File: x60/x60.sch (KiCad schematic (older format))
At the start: 1 part

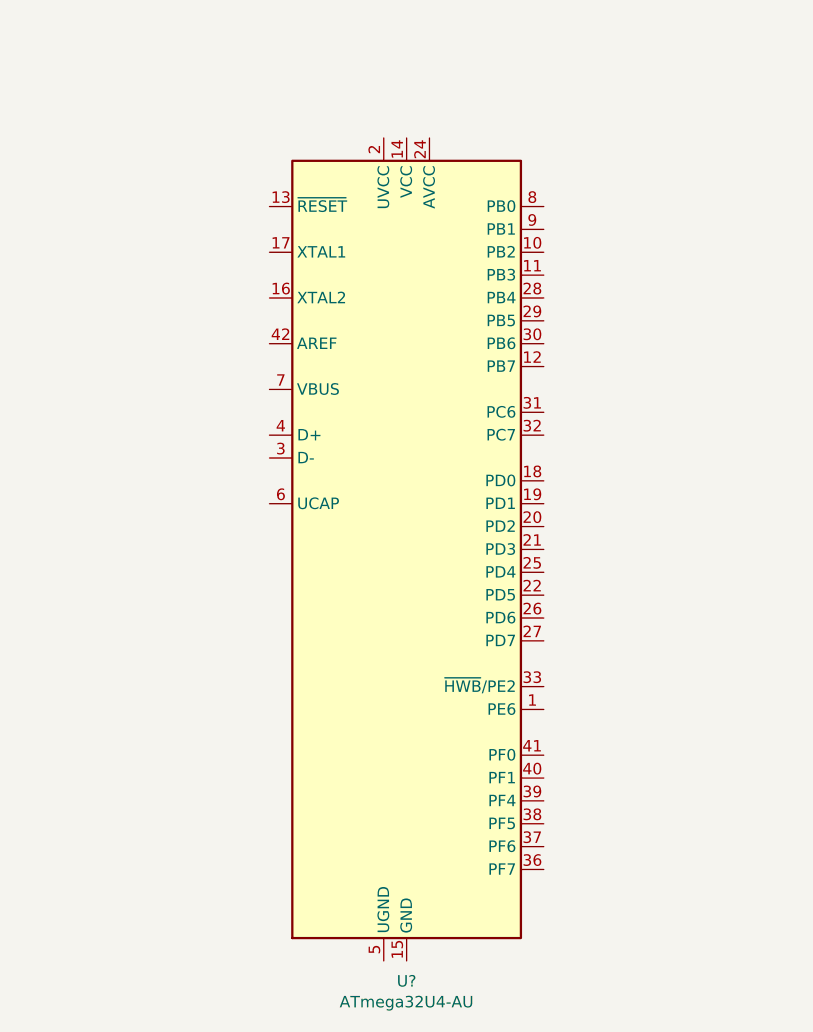
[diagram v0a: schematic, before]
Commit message: wired mcu
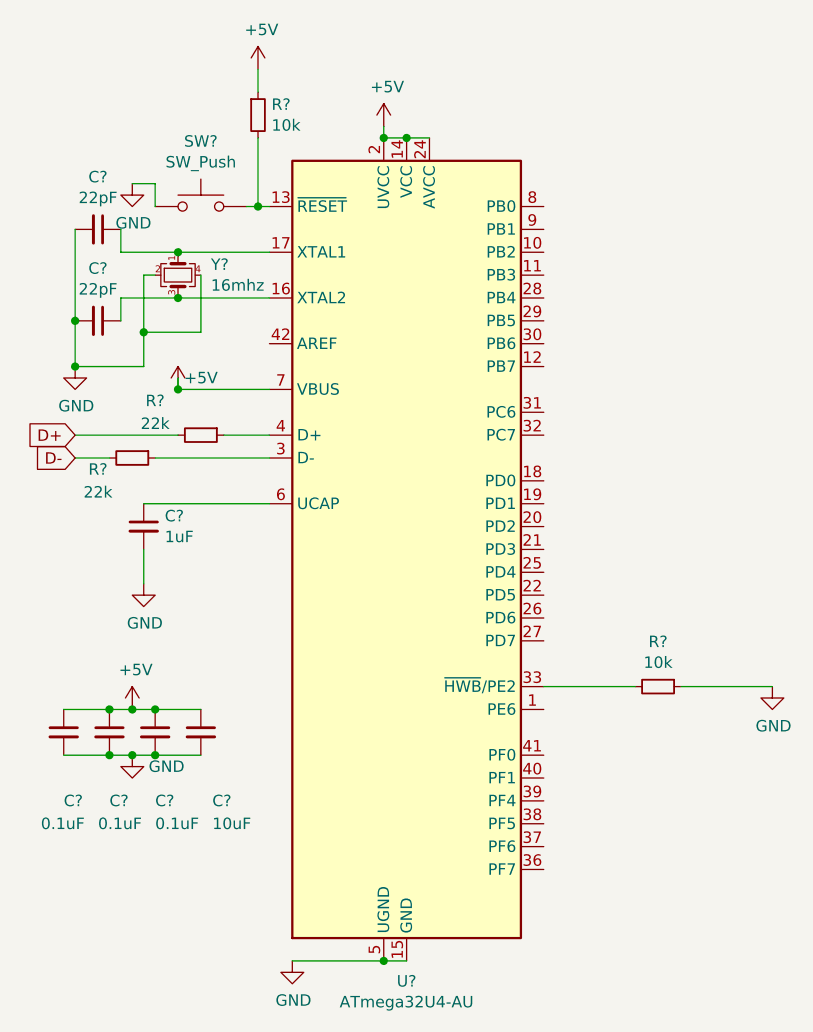
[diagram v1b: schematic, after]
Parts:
- added C?: 1uF, symbol Device:C_Small
- added C? (x3): 0.1uF, symbol Device:C_Small
- added C?: 10uF, symbol Device:C_Small
- added C? (x2): 22pF, symbol Device:C_Small
- added R? (x2): 10k, symbol Device:R_Small
- added R? (x2): 22k, symbol Device:R_Small
- added SW?: SW_Push, symbol Switch:SW_Push
- added Y?: 16mhz, symbol Device:Crystal_GND24_Small
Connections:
- net at U?.13 (~RESET): now also R?.2, SW?.2
- net +5V: now reaches U?.14 (VCC), U?.34 (VCC)
- net +5V: now also U?.2 (UVCC), U?.24 (AVCC), U?.44 (AVCC), U?.7 (VBUS), C?.1, C?.1, C?.1, C?.1, R?.1
- net GND: now reaches U?.15 (GND), U?.23 (GND), U?.35 (GND), U?.43 (GND)
- net GND: now also U?.5 (UGND), C?.2, C?.2, C?.2, C?.2, C?.2, C?.2, C?.2, R?.1, SW?.1, Y?.2, Y?.4
- net at U?.16 (XTAL2): now also C?.1, Y?.3
- net at U?.17 (XTAL1): now also C?.1, Y?.1
- net at U?.3 (D-): now also R?.1
- net at U?.33 (~HWB~/PE2): now also R?.2
- net at U?.4 (D+): now also R?.1
- net at U?.6 (UCAP): now also C?.1
- new net D+: R?.2
- new net D-: R?.2

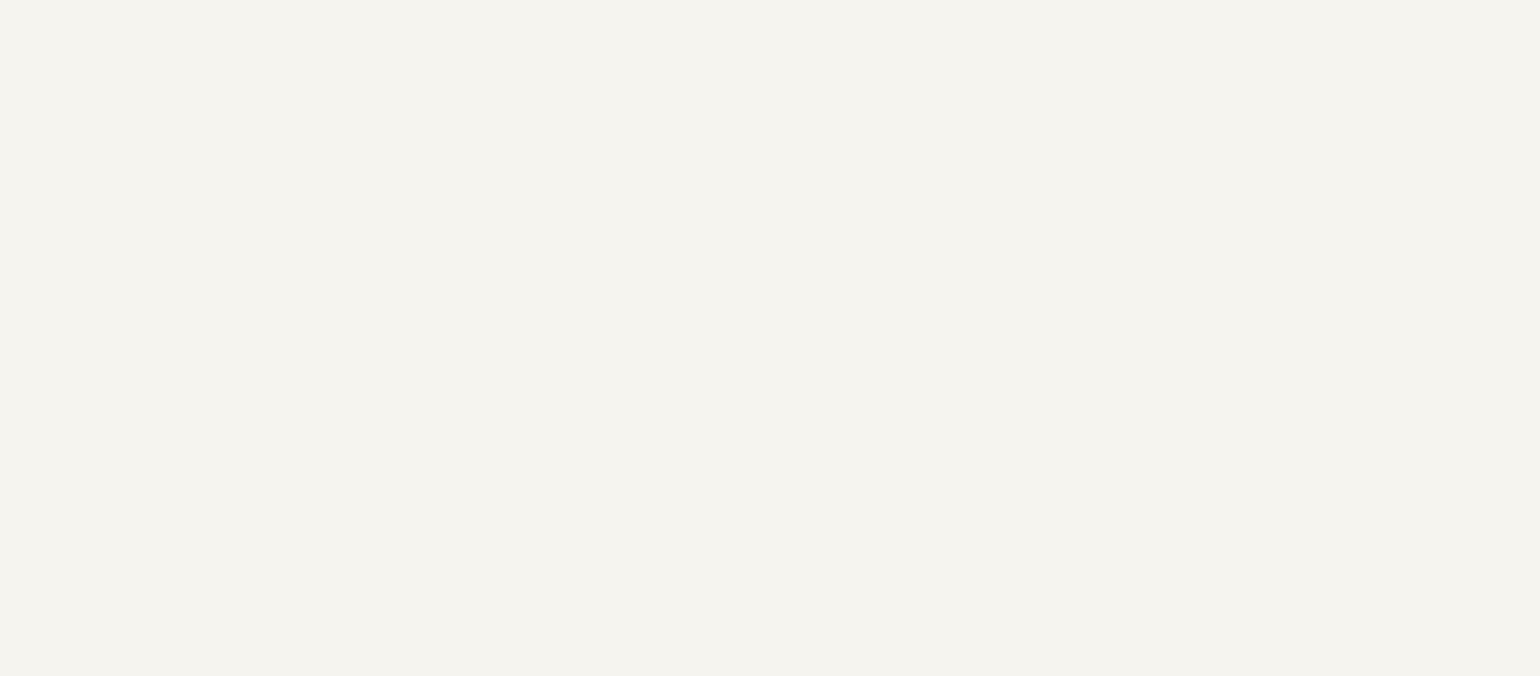
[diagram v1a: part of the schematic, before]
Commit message: added switches
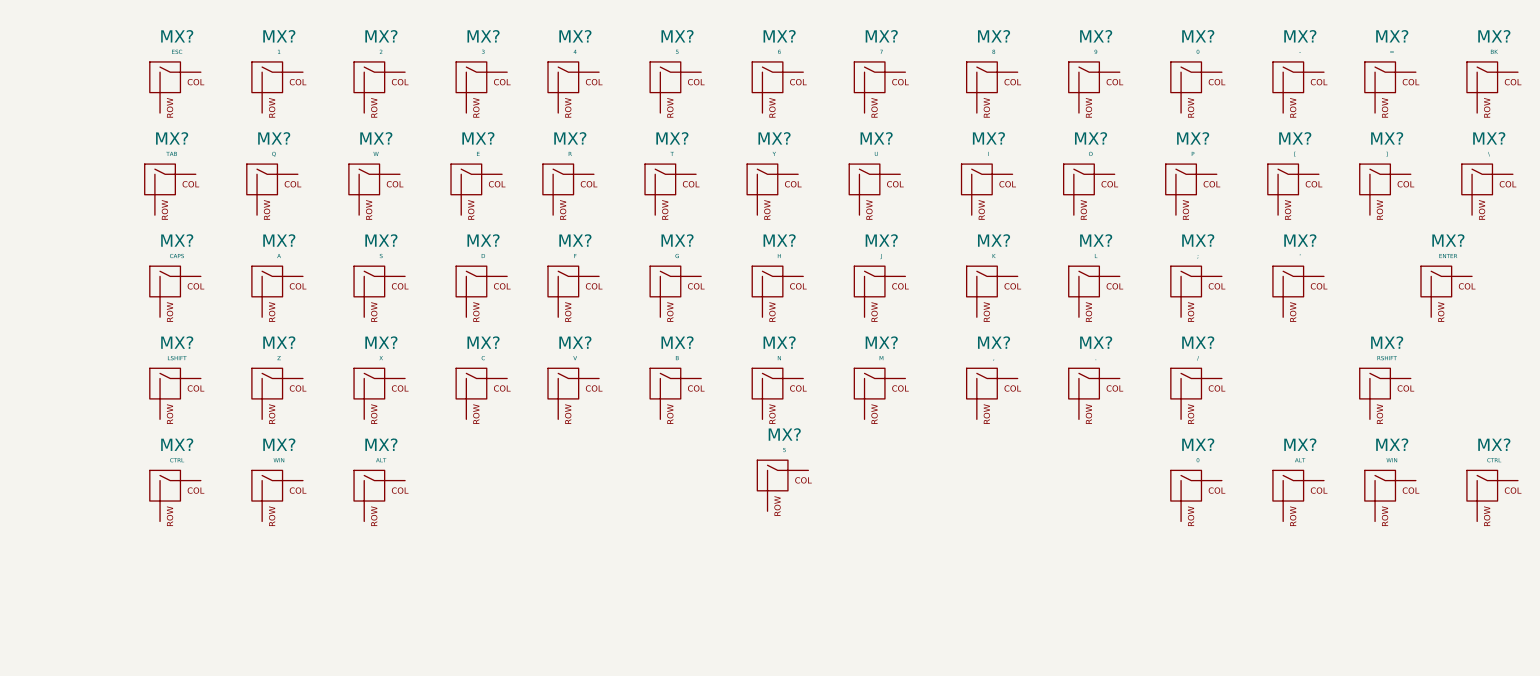
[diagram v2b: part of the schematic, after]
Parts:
- added MX?: ESC, symbol MX_Alps_Hybrid:MX-NoLED
- added MX?: 1, symbol MX_Alps_Hybrid:MX-NoLED
- added MX?: 2, symbol MX_Alps_Hybrid:MX-NoLED
- added MX?: 3, symbol MX_Alps_Hybrid:MX-NoLED
- added MX?: 4, symbol MX_Alps_Hybrid:MX-NoLED
- added MX? (x2): 5, symbol MX_Alps_Hybrid:MX-NoLED
- added MX?: 6, symbol MX_Alps_Hybrid:MX-NoLED
- added MX?: 7, symbol MX_Alps_Hybrid:MX-NoLED
- added MX?: 8, symbol MX_Alps_Hybrid:MX-NoLED
- added MX?: 9, symbol MX_Alps_Hybrid:MX-NoLED
- added MX? (x2): 0, symbol MX_Alps_Hybrid:MX-NoLED
- added MX?: -, symbol MX_Alps_Hybrid:MX-NoLED
- added MX?: =, symbol MX_Alps_Hybrid:MX-NoLED
- added MX?: BK, symbol MX_Alps_Hybrid:MX-NoLED
- added MX?: TAB, symbol MX_Alps_Hybrid:MX-NoLED
- added MX?: Q, symbol MX_Alps_Hybrid:MX-NoLED
- added MX?: W, symbol MX_Alps_Hybrid:MX-NoLED
- added MX?: E, symbol MX_Alps_Hybrid:MX-NoLED
- added MX?: R, symbol MX_Alps_Hybrid:MX-NoLED
- added MX?: T, symbol MX_Alps_Hybrid:MX-NoLED
- added MX?: Y, symbol MX_Alps_Hybrid:MX-NoLED
- added MX?: U, symbol MX_Alps_Hybrid:MX-NoLED
- added MX?: I, symbol MX_Alps_Hybrid:MX-NoLED
- added MX?: O, symbol MX_Alps_Hybrid:MX-NoLED
- added MX?: P, symbol MX_Alps_Hybrid:MX-NoLED
- added MX?: [, symbol MX_Alps_Hybrid:MX-NoLED
- added MX?: ], symbol MX_Alps_Hybrid:MX-NoLED
- added MX?: \\, symbol MX_Alps_Hybrid:MX-NoLED
- added MX?: CAPS, symbol MX_Alps_Hybrid:MX-NoLED
- added MX?: A, symbol MX_Alps_Hybrid:MX-NoLED
- added MX?: S, symbol MX_Alps_Hybrid:MX-NoLED
- added MX?: D, symbol MX_Alps_Hybrid:MX-NoLED
- added MX?: F, symbol MX_Alps_Hybrid:MX-NoLED
- added MX?: G, symbol MX_Alps_Hybrid:MX-NoLED
- added MX?: H, symbol MX_Alps_Hybrid:MX-NoLED
- added MX?: J, symbol MX_Alps_Hybrid:MX-NoLED
- added MX?: K, symbol MX_Alps_Hybrid:MX-NoLED
- added MX?: L, symbol MX_Alps_Hybrid:MX-NoLED
- added MX?: ;, symbol MX_Alps_Hybrid:MX-NoLED
- added MX?: ', symbol MX_Alps_Hybrid:MX-NoLED
- added MX?: ENTER, symbol MX_Alps_Hybrid:MX-NoLED
- added MX?: LSHIFT, symbol MX_Alps_Hybrid:MX-NoLED
- added MX?: Z, symbol MX_Alps_Hybrid:MX-NoLED
- added MX?: X, symbol MX_Alps_Hybrid:MX-NoLED
- added MX?: C, symbol MX_Alps_Hybrid:MX-NoLED
- added MX?: V, symbol MX_Alps_Hybrid:MX-NoLED
- added MX?: B, symbol MX_Alps_Hybrid:MX-NoLED
- added MX?: N, symbol MX_Alps_Hybrid:MX-NoLED
- added MX?: M, symbol MX_Alps_Hybrid:MX-NoLED
- added MX?: ,, symbol MX_Alps_Hybrid:MX-NoLED
- added MX?: ., symbol MX_Alps_Hybrid:MX-NoLED
- added MX?: /, symbol MX_Alps_Hybrid:MX-NoLED
- added MX?: RSHIFT, symbol MX_Alps_Hybrid:MX-NoLED
- added MX? (x2): CTRL, symbol MX_Alps_Hybrid:MX-NoLED
- added MX? (x2): WIN, symbol MX_Alps_Hybrid:MX-NoLED
- added MX? (x2): ALT, symbol MX_Alps_Hybrid:MX-NoLED

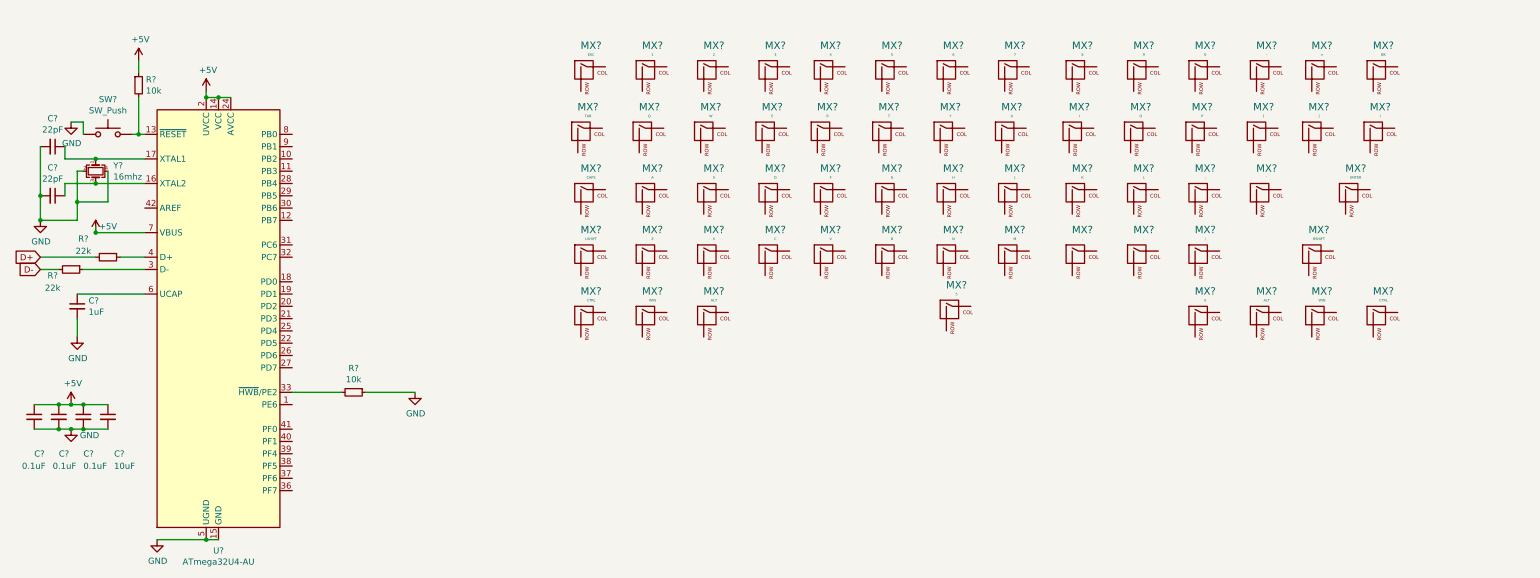
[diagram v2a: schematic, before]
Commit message: updated wiring
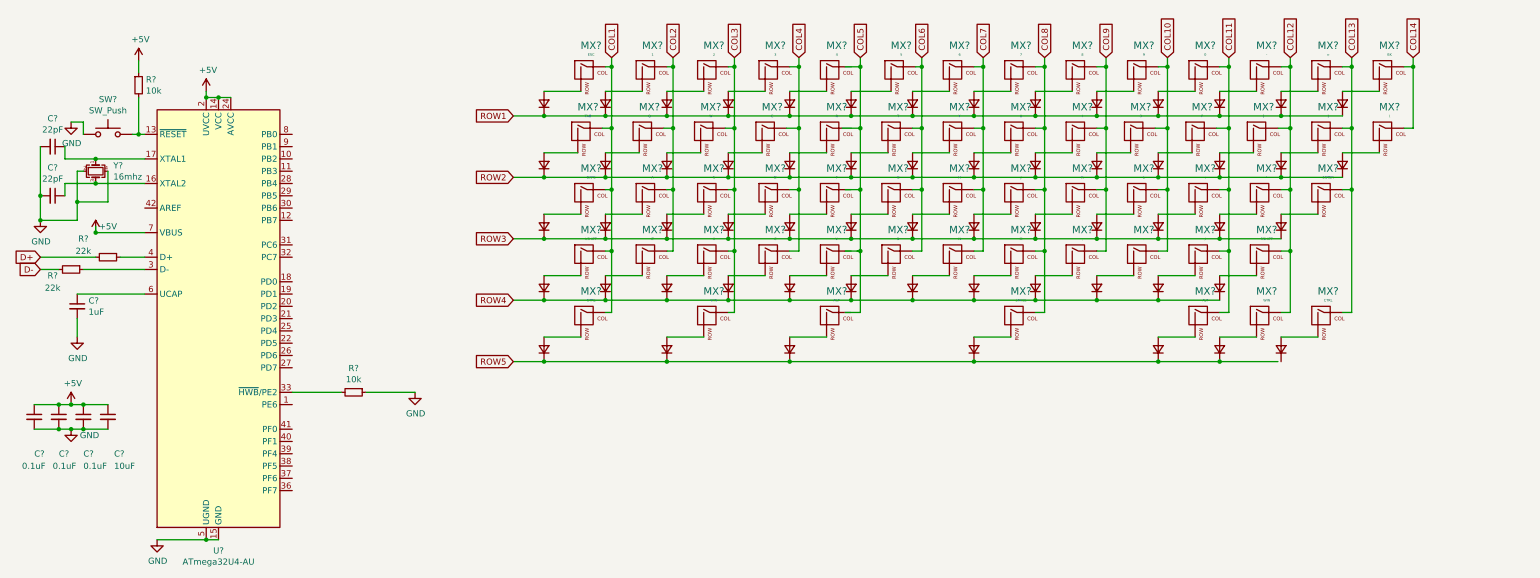
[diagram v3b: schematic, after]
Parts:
- removed MX?: 0, symbol MX_Alps_Hybrid:MX-NoLED
- added D? (x60): D_Small, symbol Device:D_Small
- MX?: value 5 -> SPACE
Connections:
- net labels added: COL1, COL10, COL11, COL12, COL13, COL14, COL2, COL3, COL4, COL5, COL6, COL7, COL8, COL9, ROW1, ROW2, ROW3, ROW4, ROW5
- wire segments 43 -> 284
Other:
- moved on the sheet: MX?

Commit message: added support for split rs/bs
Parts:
- added D61, D62: D_Small, symbol Device:D_Small
- added MX58: RSHIFT_1.75, symbol MX_Alps_Hybrid:MX-NoLED
- added MX62: FN, symbol MX_Alps_Hybrid:MX-NoLED
- added MX63: \\, symbol MX_Alps_Hybrid:MX-NoLED
- added MX64: `, symbol MX_Alps_Hybrid:MX-NoLED
- gave numbers to parts that had none: 134
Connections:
- wire segments 284 -> 302

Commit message: started designing pcb
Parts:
- C1, C2, C3, C4, C5, C6, C7: footprint (none) -> Capacitor_SMD:C_0805_2012Metric
- D1, D10, D11, D12, D13, D14, D15, D16, D17, D18, D19, D2, D20, D21, D22, D23, D24, D25, D26, D27, D28, D29, D3, D30, D31, D32, D33, D34, D35, D36, D37, D38, D39, D4, D40, D41, D42, D43, D44, D45, D46, D47, D48, D49, D5, D50, D51, D52, D53, D54, D55, D56, D57, D58, D59, D6, D60, D61, D62, D7, D8, D9: footprint (none) -> Diode_SMD:D_SOD-123
- MX1, MX10, MX11, MX12, MX13, MX14, MX15, MX16, MX17, MX18, MX19, MX2, MX20, MX21, MX22, MX23, MX24, MX25, MX26, MX27, MX28, MX29, MX3, MX30, MX31, MX32, MX33, MX34, MX35, MX36, MX37, MX38, MX39, MX4, MX40, MX41, MX42, MX43, MX44, MX45, MX46, MX47, MX48, MX49, MX5, MX50, MX51, MX52, MX53, MX54, MX55, MX56, MX57, MX58, MX59, MX6, MX60, MX61, MX62, MX63, MX64, MX7, MX8, MX9: footprint (none) -> MX_Alps_Hybrid:MX-1U-NoLED
- R1, R2, R3, R4: footprint (none) -> Resistor_SMD:R_0805_2012Metric
- SW1: footprint (none) -> random-keyboard-parts:SKQG-1155865
- Y1: footprint (none) -> Crystal:Crystal_SMD_3225-4Pin_3.2x2.5mm
